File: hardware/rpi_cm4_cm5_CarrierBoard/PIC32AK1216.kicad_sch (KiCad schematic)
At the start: 82 parts, among them J10 PR20206VBNN, U28 PIC32AK1216GC41064-I/M7, Y3 20MHz

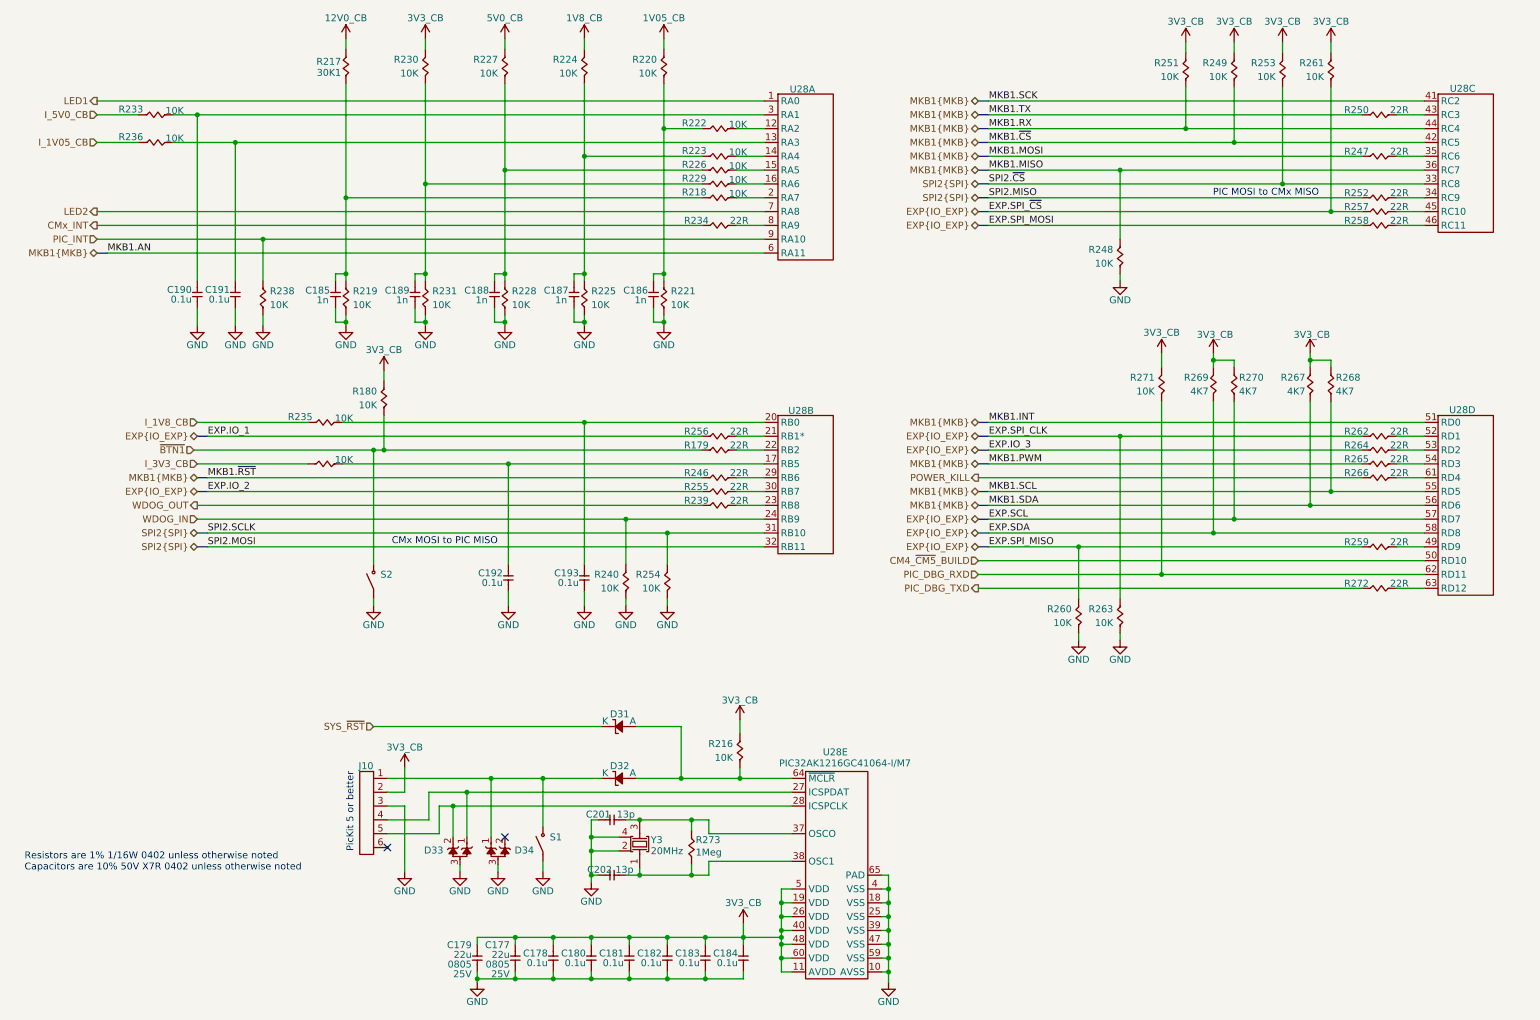
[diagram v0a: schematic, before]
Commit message: Preliminary completion of RPI CMx schematics Cleaned up hierarchical root page
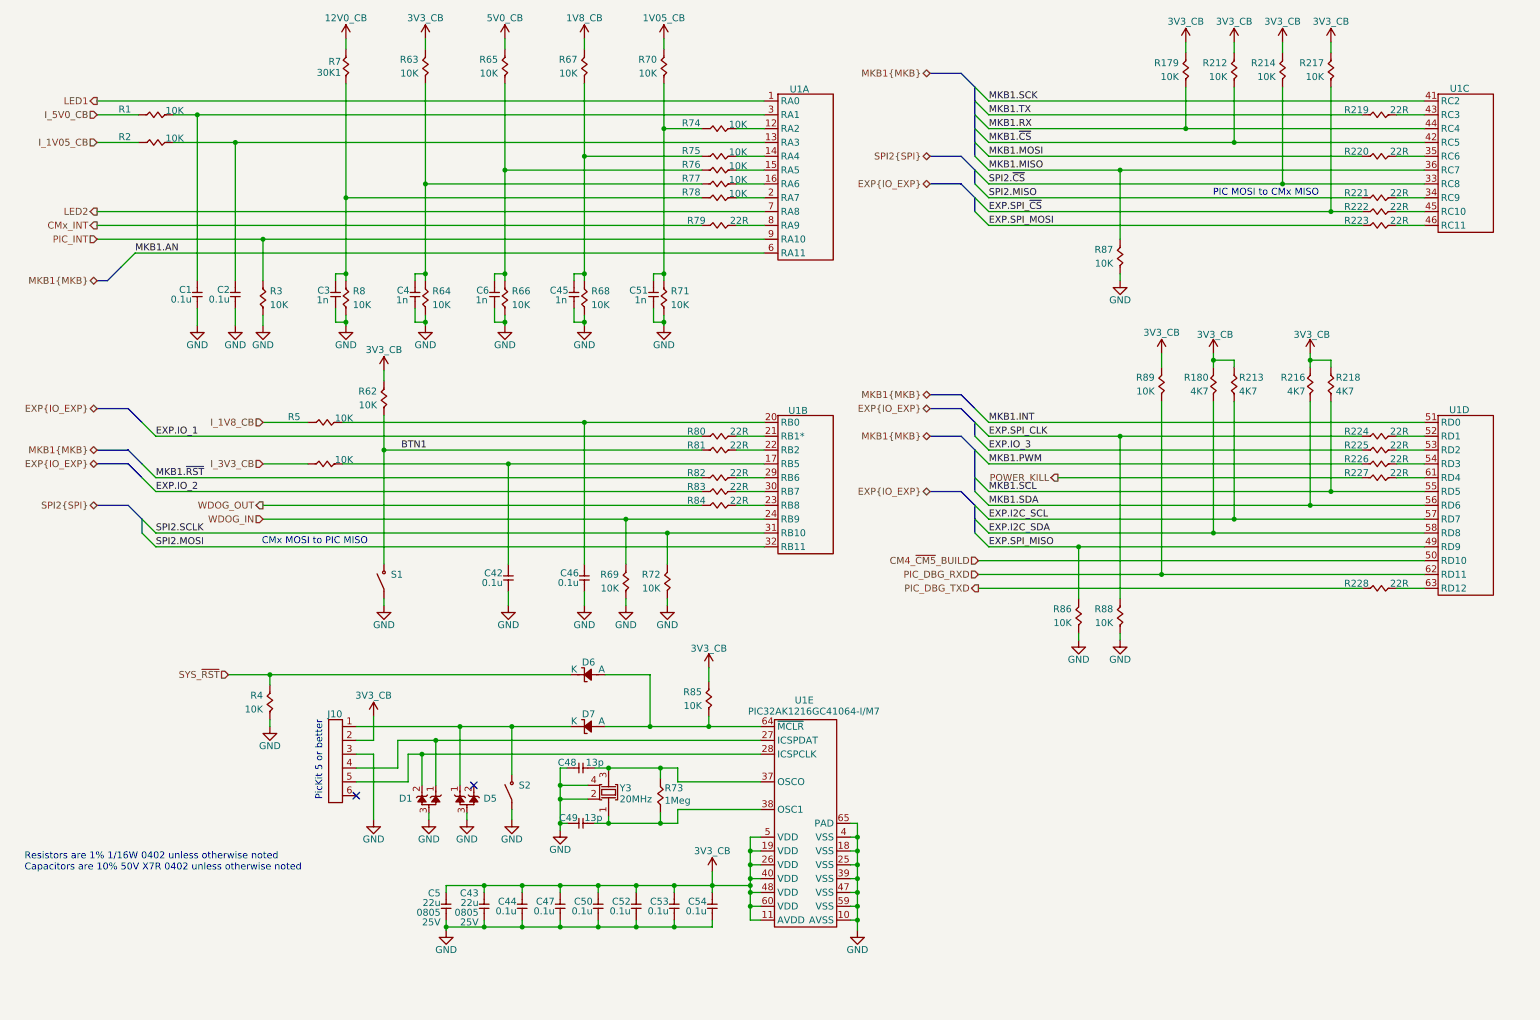
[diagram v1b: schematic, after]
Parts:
- removed R259: 22R, footprint:RES_0402, symbol KicadCompDb:Resistors/RES_SMT_00015
- added R4: 10K, footprint:RES_0402, symbol KicadCompDb:Resistors/RES_SMT_00013
- renumbered C190 to C1, C191 to C2, C185 to C3, C189 to C4, C192 to C42, C177 to C43, C178 to C44, C187 to C45, C193 to C46, C180 to C47, C201 to C48, C202 to C49, C179 to C5, C181 to C50, C186 to C51, C182 to C52, C183 to C53, C184 to C54, C188 to C6, D33 to D1, D34 to D5, D31 to D6, D32 to D7, R233 to R1, R251 to R179, R269 to R180, R236 to R2, R249 to R212, R270 to R213, R253 to R214, R267 to R216, R261 to R217, R268 to R218, R250 to R219, R247 to R220, R252 to R221, R257 to R222, R258 to R223, R262 to R224, R264 to R225, R265 to R226, R266 to R227, R272 to R228, R238 to R3, R235 to R5, R237 to R6, R180 to R62, R230 to R63, R231 to R64, R227 to R65, R228 to R66, R224 to R67, R225 to R68, R240 to R69, R217 to R7, R220 to R70, R221 to R71, R254 to R72, R273 to R73, R222 to R74, R223 to R75, R226 to R76, R229 to R77, R218 to R78, R234 to R79, R219 to R8, R256 to R80, R179 to R81, R246 to R82, R255 to R83, R239 to R84, R216 to R85, R260 to R86, R248 to R87, R263 to R88, R271 to R89, S2 to S1, S1 to S2, U28 to U1
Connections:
- net EXP.SPI_MISO: now also U1.49 (RD9)
- net GND: now also R4.1
- net SYS_~{RST}: now also R4.2
- net EXP.SCL renamed EXP.I2C_SCL
- net EXP.SDA renamed EXP.I2C_SDA
- net ~{BTN1} renamed BTN1
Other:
- moved on the sheet: C43, C44, C47, C48, C49, C5, C50, C52, C53, C54, D1, D5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

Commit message: Add preliminary BOM and preliminary .pdf schmematics Add BOM option for I2C control of ILI2132A for CapTouch HMI Add BOM options and DNP / 0R resistors for CM4 - CM5 build options
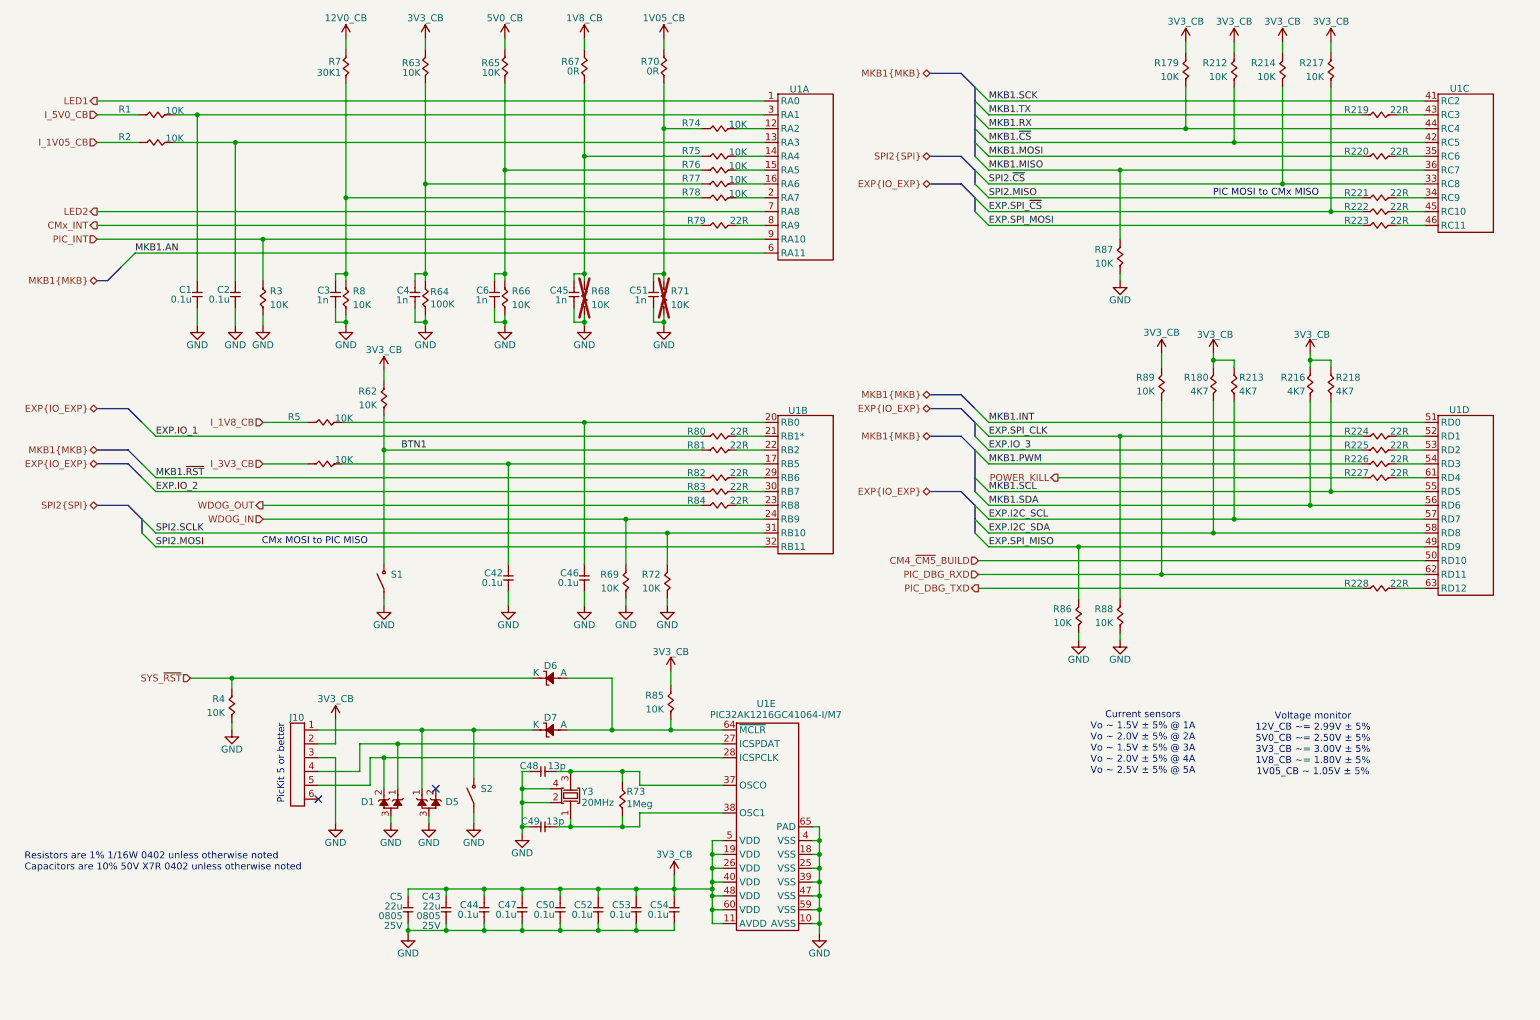
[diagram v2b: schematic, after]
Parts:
- removed R64, R67, R70: 10K, footprint:RES_0402, symbol KicadCompDb:Resistors/RES_SMT_00013
- added R64: 100K, footprint:RES_0402, symbol KicadCompDb:Resistors/RES_SMT_00018
- added R67, R70: 0R, footprint:RES_0402, symbol KicadCompDb:Resistors/RES_SMT_00001
- R68, R71: now not fitted
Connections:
- net 1V05_CB: now also R70.2
- net 1V8_CB: now also R67.2
- net GND: now also R64.1
- net at C45.2, R68.2, R75.2: now also R67.1
- net at C4.2, R63.1, R77.2: now also R64.2
- net at C51.2, R71.2, R74.2: now also R70.1
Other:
- note added: "Current sensors Vo ~ 1.5V ± 5% @ 1A Vo ~ 2.0V ± 5% @ 2A Vo ~ 1.5V ± 5% @ 3A Vo ~ 2.0V ± 5% @ 4A Vo ~ 2.5V ± 5% @ 5A"
- note added: "Voltage monitor 12V_CB ~= 2.99V ± 5% 5V0_CB ~= 2.50V ± 5% 3V3_CB ~= 3.00V ± 5% 1V8_CB ~= 1.80V ± 5% 1V05_CB ~ 1.05V ± 5%"
- moved on the sheet: C43, C44, C47, C48, C49, C5, C50, C52, C53, C54, D1, D5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

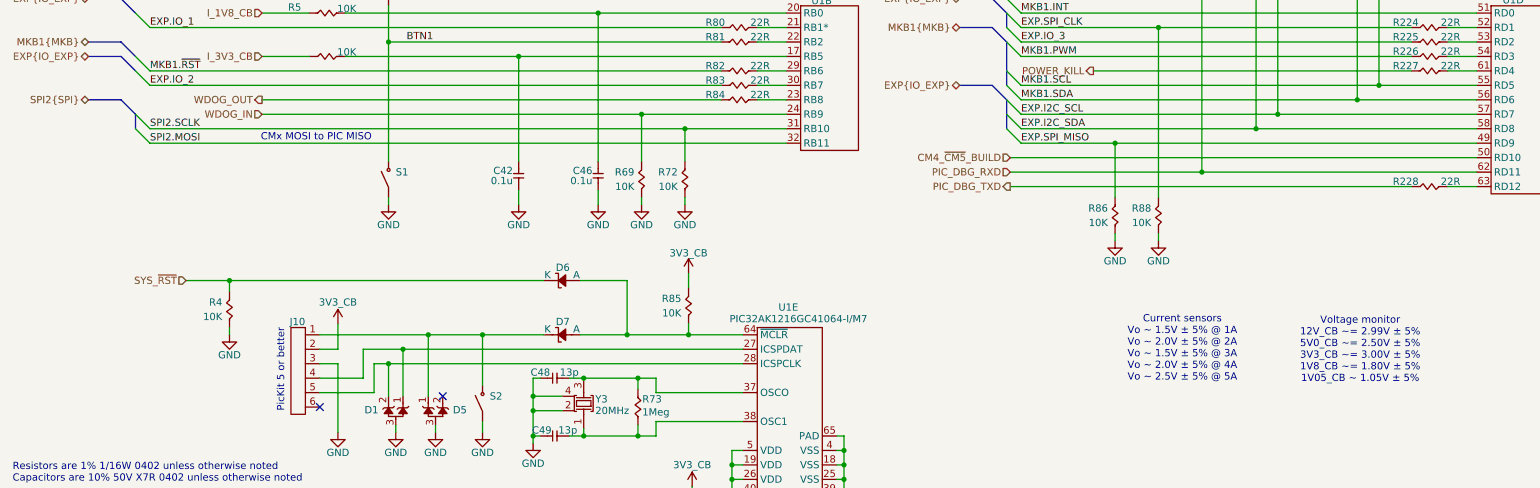
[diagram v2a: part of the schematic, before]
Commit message: Added power input protection & filter Added dedicated QWIIC connector on RPI CMx I2C6 bus Adjusted power table and PinMux Updated schematics accordingly
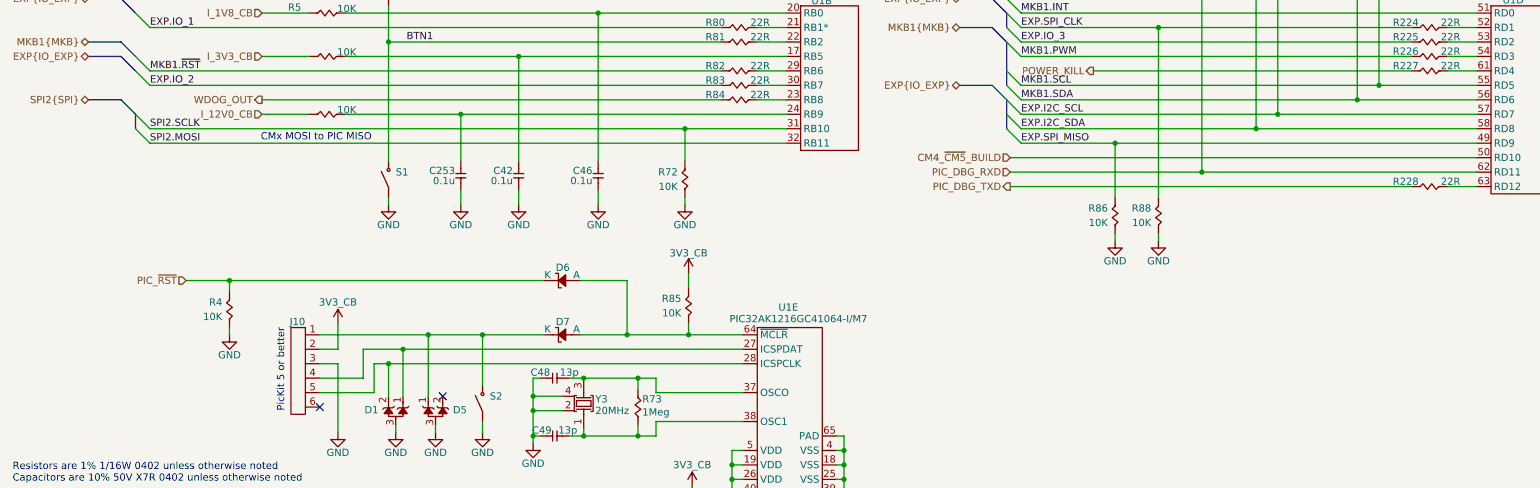
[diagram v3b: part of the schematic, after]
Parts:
- added C253: 0.1u, footprint:CAP_NONPOL_0402, symbol KicadCompDb:Capacitors/CAP_CER_SMT_00001
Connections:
- net GND: now also C253.1; no longer R69.1
- net SYS_~{RST} renamed PIC_~{RST}
- net WDOG_IN: no longer names the net of U1.24 (RB9)
- net WDOG_IN: now also R69.1, C253.2; no longer R69.2
- new net I_12V0_CB: R69.2
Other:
- note removed: "Current sensors Vo ~ 1.5V ± 5% @ 1A Vo ~ 2.0V ± 5% @ 2A Vo ~ 1.5V ± 5% @ 3A Vo ~ 2.0V ± 5% @ 4A Vo ~ 2.5V ± 5% @ 5A"
- note removed: "Voltage monitor 12V_CB ~= 2.99V ± 5% 5V0_CB ~= 2.50V ± 5% 3V3_CB ~= 3.00V ± 5% 1V8_CB ~= 1.80V ± 5% 1V05_CB ~ 1.05V ± 5%"

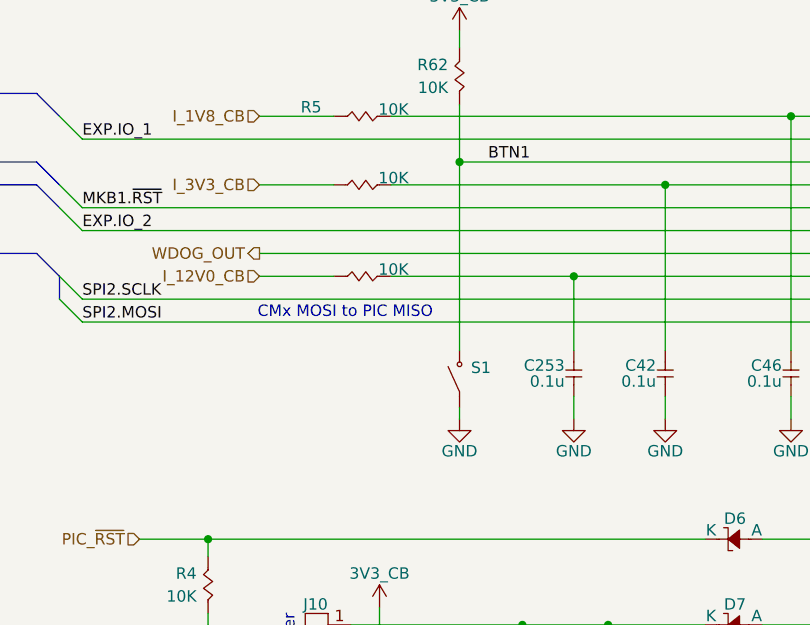
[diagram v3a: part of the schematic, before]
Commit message: Update watchdog timer circuit to add external watchdog timer IC to be fed by PIC Adjust reset scheme in power supply sheet accordingly Adjust PinMux, regen BOM and PDF schematics (preliminary) Start preliminary component placement in the PCB
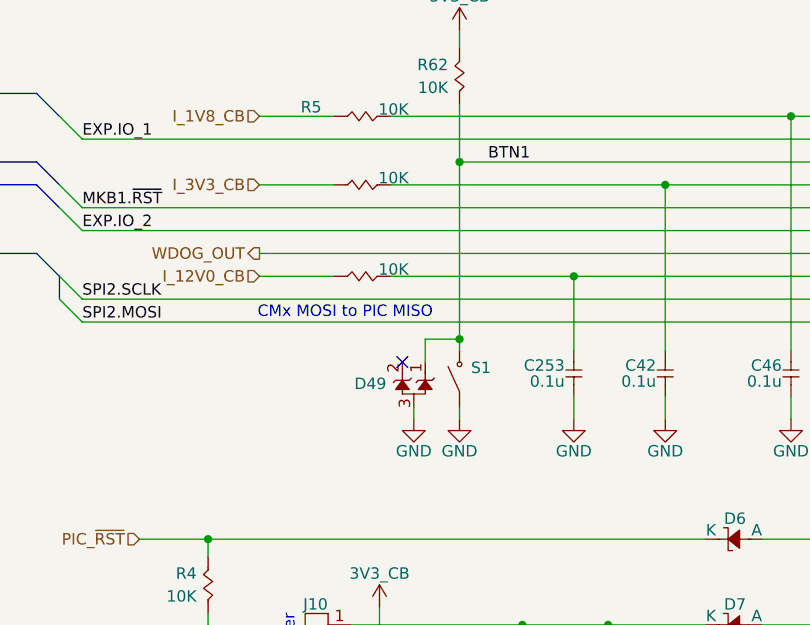
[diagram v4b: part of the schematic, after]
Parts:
- added D49: D1213A-02SOL-7, footprint:SOT-23-3, symbol KicadCompDb:ESD Diodes/ESD_DIODE_00002
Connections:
- net BTN1: now also D49.1
- net GND: now also D49.3 (GND)
- no-connect marks 2 -> 3
